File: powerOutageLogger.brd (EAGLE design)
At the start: 99.1 x 74.9 mm, 38 parts, among them J1 2.1MMJACKTHM, U1 ATmega328P, U2 78L05, U3 DS18B20, Y1 16MHz

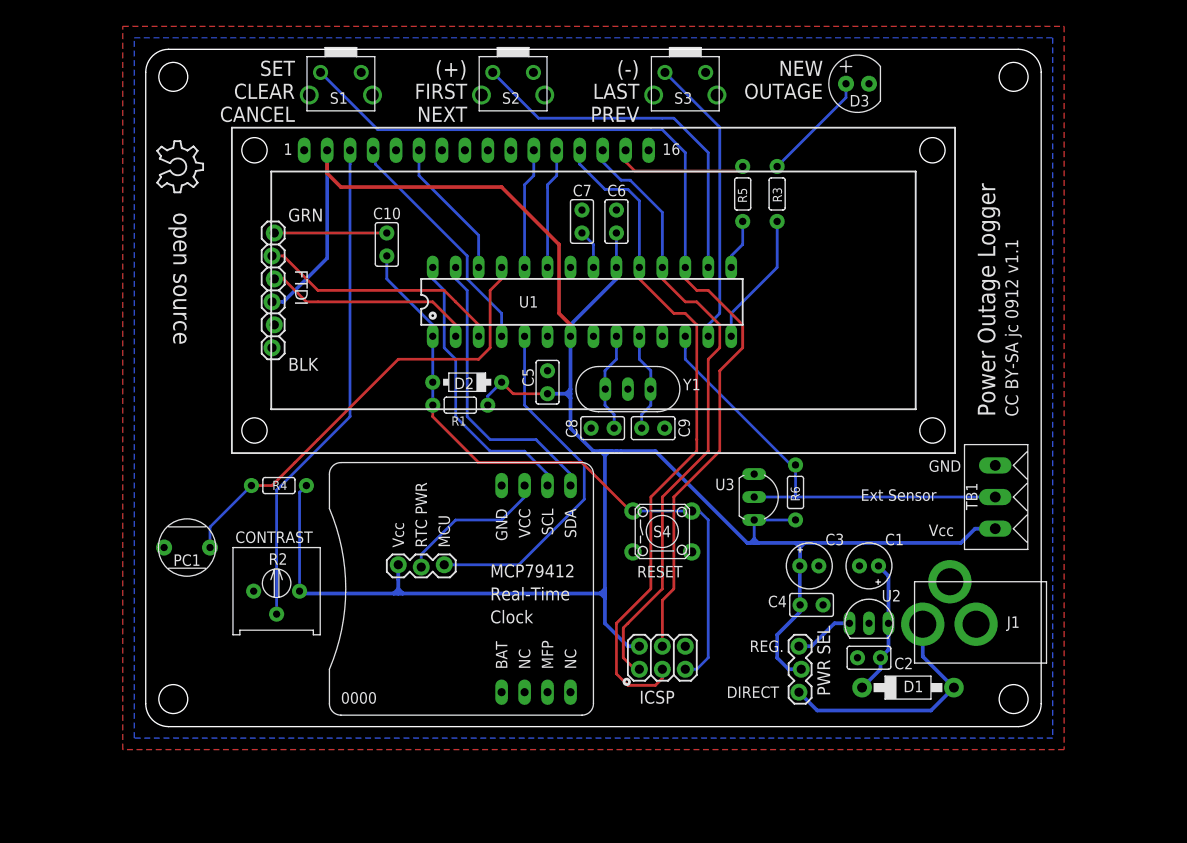
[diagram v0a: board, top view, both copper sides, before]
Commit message: Minor routing changes, fix hyperlinks in ReadMe.txt.
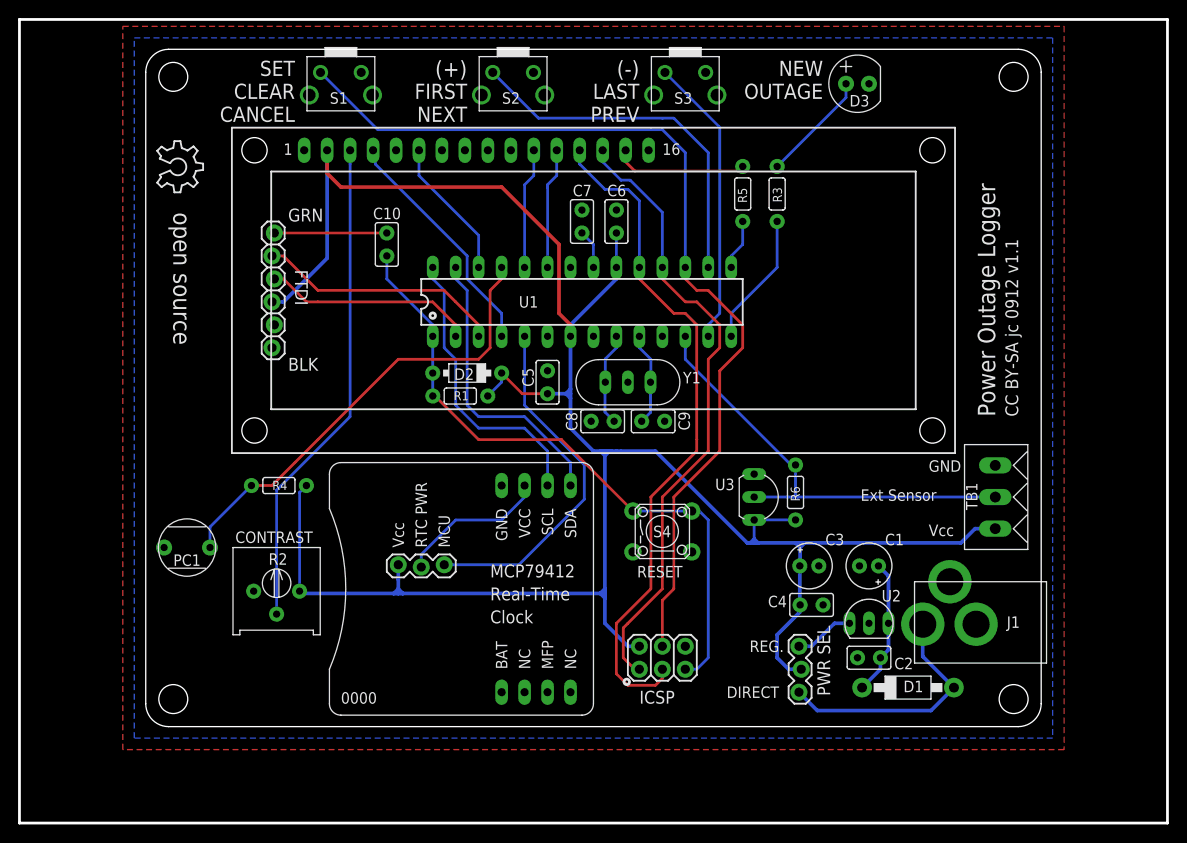
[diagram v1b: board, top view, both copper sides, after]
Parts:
- moved D2 1.02 mm to (35.6, 39.1)
- moved R1 1.02 mm to (34.8, 36.6)
- moved Y1 0.76 mm to (53.3, 38.1)
- moved C8 0.76 mm to (50.5, 33.8)
- moved C9 0.76 mm to (56.1, 33.8)
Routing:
- net /RESET: track 73.4 -> 72.1 mm
- net XTAL2: track 11.1 -> 10.3 mm
- net XTAL1: track 11.1 -> 10.3 mm
- net SCL: track 31.6 -> 32.4 mm
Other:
- board size 99.1 x 74.9 mm -> 127 x 88.9 mm
